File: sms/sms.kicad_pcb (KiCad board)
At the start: 2 copper layers, 17.5 x 65 mm, 3 parts, among them J1 Sega_GG_Cartridge, J2 Sega_SMS_Cartridge

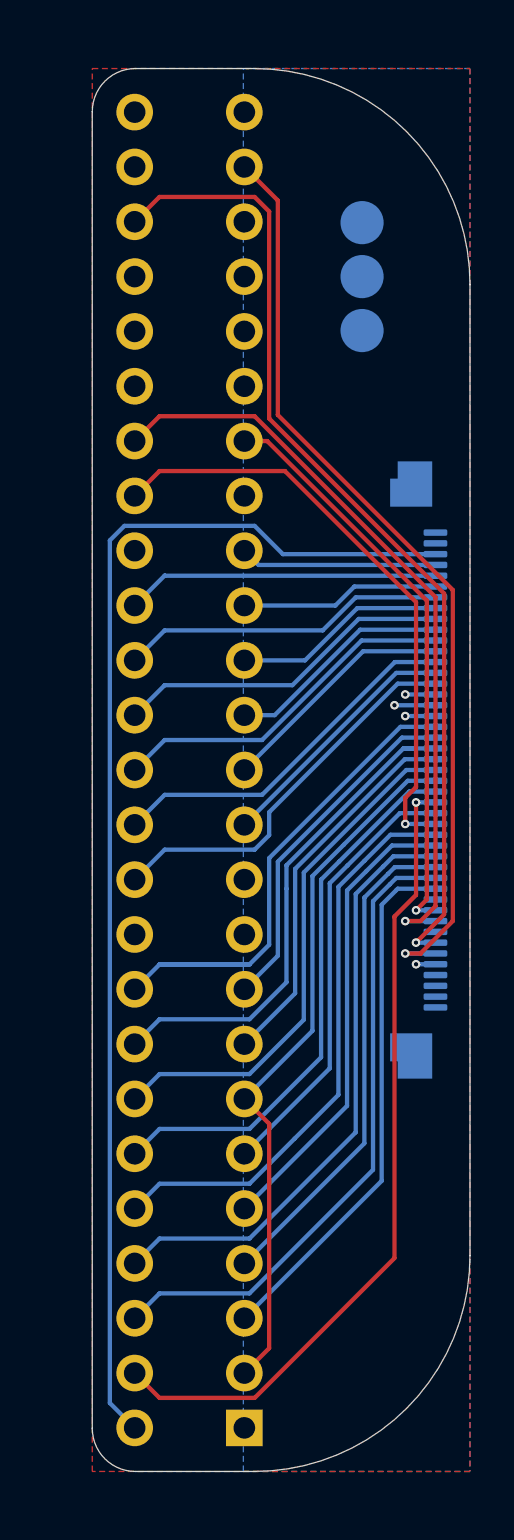
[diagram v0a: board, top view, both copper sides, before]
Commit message: Widen via holes
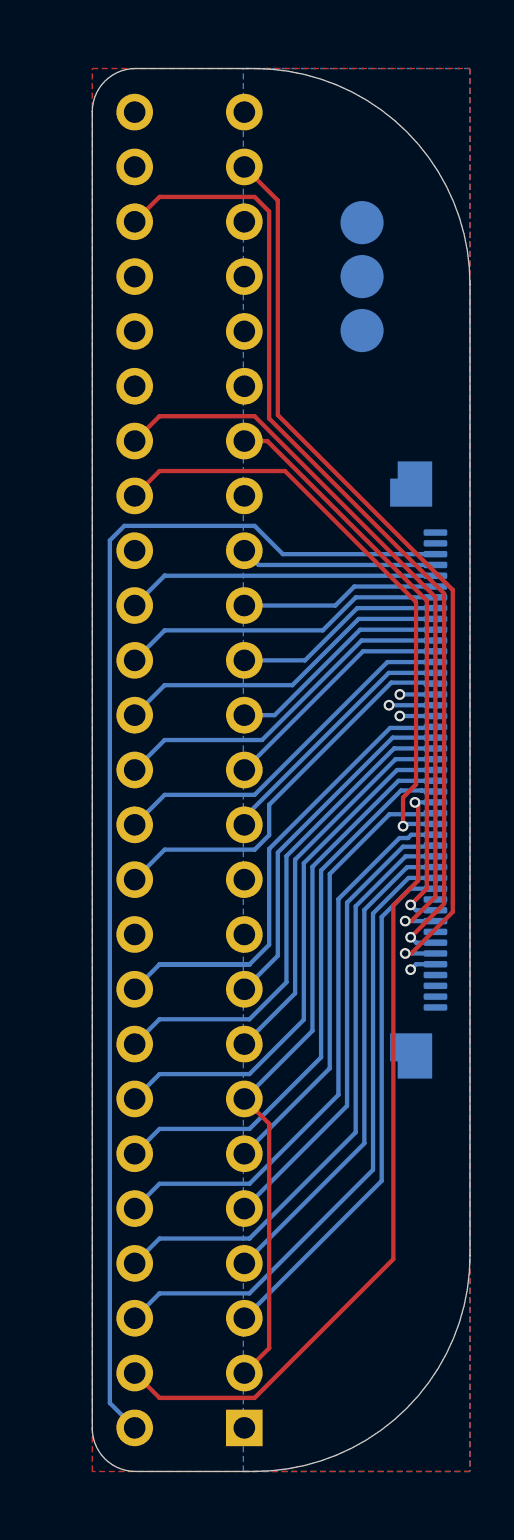
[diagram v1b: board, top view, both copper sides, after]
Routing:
- net GND: track 5.60 -> 6.70 mm

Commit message: Fix SMS pin ordering
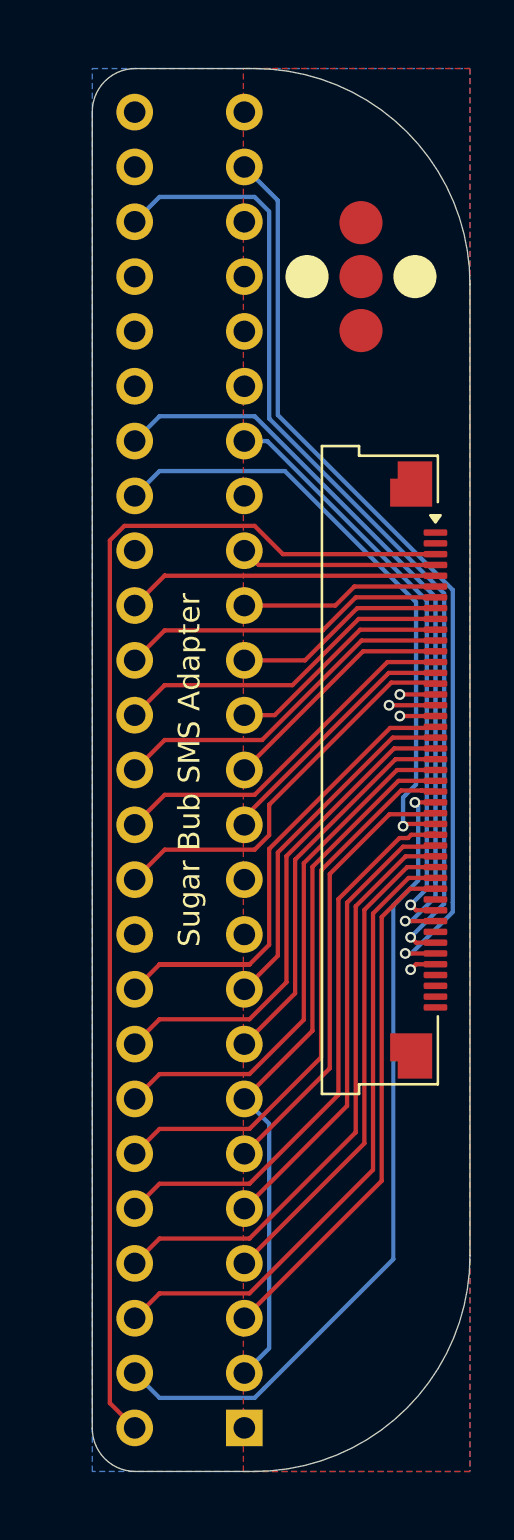
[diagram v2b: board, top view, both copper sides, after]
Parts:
- J1: footprint SugarBub:Amphenol_F32Q-1A7x1-11045_1x45-1MP_P0.5mm_HorizontalReversed -> Connector_FFC-FPC:Amphenol_F32Q-1A7x1-11045_1x45-1MP_P0.5mm_Horizontal; moved to F.Cu
- TP1: moved to F.Cu
- turned J1 to -90 degrees
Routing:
- added copper zone on F.Cu, net +5V
- added copper zone on B.Cu, net GND
- removed copper zone on B.Cu, net +5V
- removed copper zone on F.Cu, net GND

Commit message: Redo SMS adapter
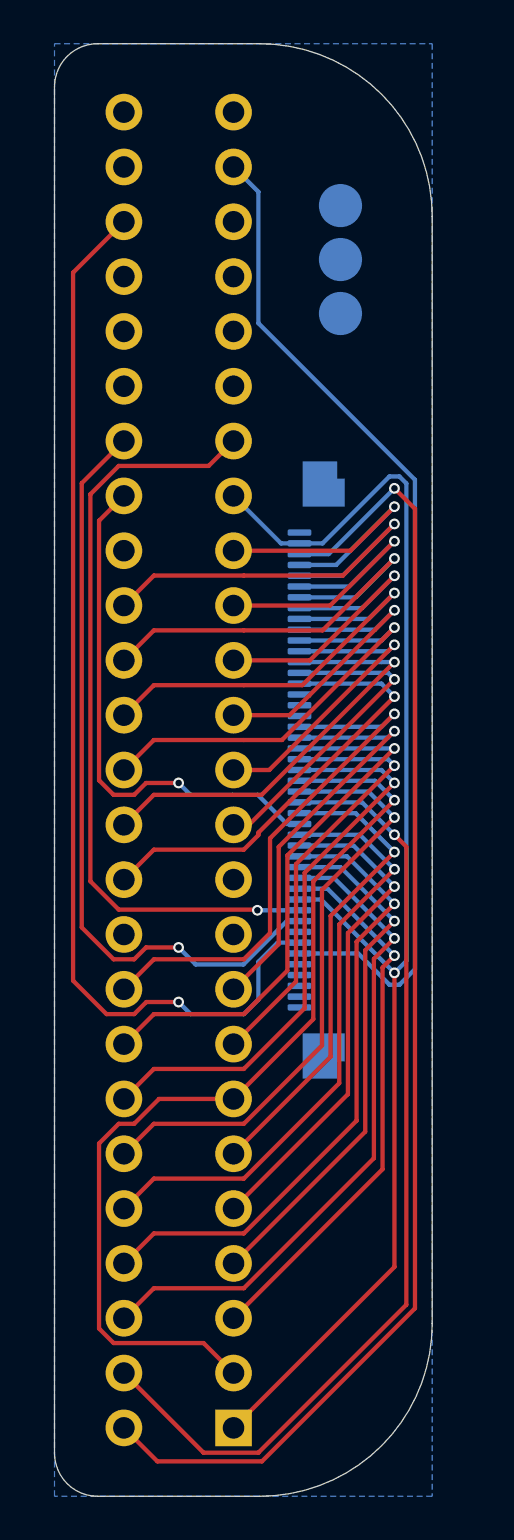
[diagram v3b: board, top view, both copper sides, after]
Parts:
- J1, TP1: moved to B.Cu
- moved TP1 1.24 mm to (109.5, 76.3)
- moved J1 0.50 mm to (110.5, 100.0)
- moved J2 0.50 mm to (104.5, 130.5)
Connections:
- J1 pad 42: +5V -> unconnected-(J1-Pin_42-Pad42)
- J1 pad 43: +5V -> unconnected-(J1-Pin_43-Pad43)
- TP1 pad 1: +5V -> unconnected-(TP1-Pad1)
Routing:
- net +5V: track 0.00 -> 63.2 mm, vias 0 -> 1
- net /CE: track 33.1 -> 44.4 mm, vias 0 -> 1
- net /M1: track 27.2 -> 35.8 mm
- net /RD: track 37.8 -> 44.5 mm
- net GND: track 6.70 -> 0.00 mm, vias 4 -> 0
- net /A7: track 14.5 -> 19.5 mm, vias 0 -> 1
- net /A6: track 9.22 -> 14.0 mm, vias 0 -> 1
- net /A12: track 9.13 -> 13.8 mm, vias 0 -> 1
- net /A5: track 15.1 -> 19.6 mm, vias 0 -> 1
- net /RST: track 45.9 -> 50.1 mm
- net /A4: track 9.86 -> 14.1 mm, vias 0 -> 1
- net /A3: track 15.8 -> 19.8 mm, vias 0 -> 1
- net CLK: track 42.9 -> 46.9 mm, vias 1 -> 0
- net /A15: track 28.2 -> 24.2 mm
- net /A2: track 10.5 -> 14.2 mm, vias 0 -> 1
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- removed copper zone on F.Cu, net +5V
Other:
- board size 17.5 x 65 mm -> 17.5 x 67.3 mm

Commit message: Add /Refresh to SMS and shrink logo
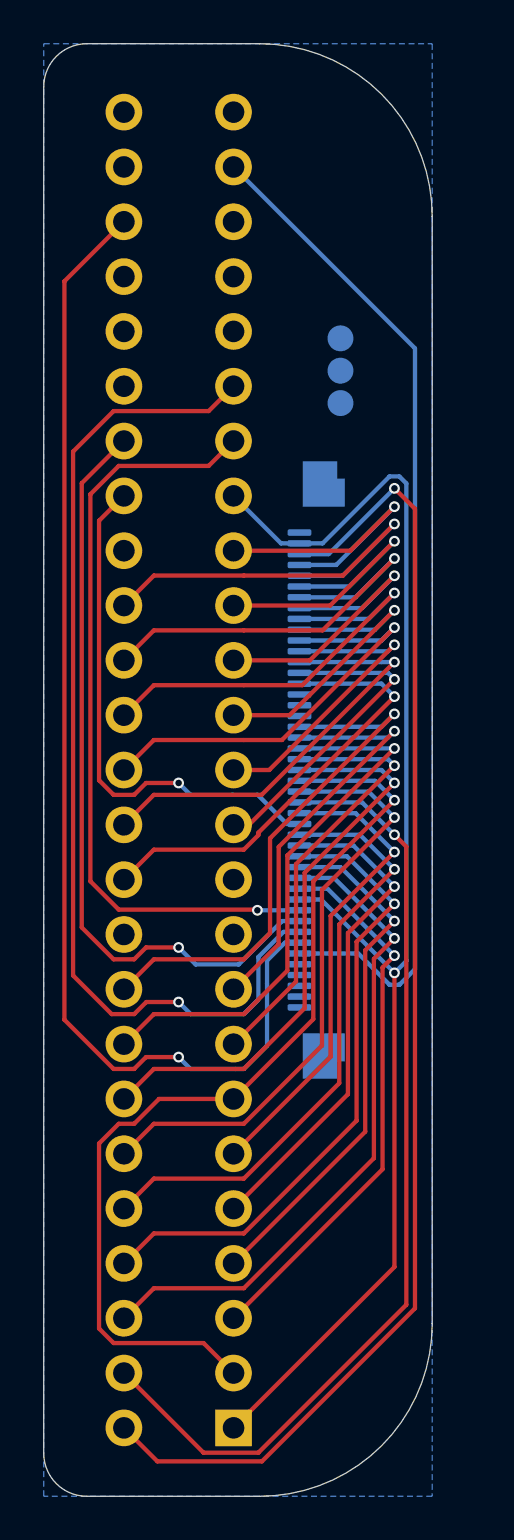
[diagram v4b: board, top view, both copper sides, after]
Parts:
- TP1: footprint SugarBub:SugarBub_Symbol -> SugarBub:SugarBub_Symbol_4.2mm
- moved TP1 5.15 mm to (109.5, 81.5), turned to -90 degrees
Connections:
- J1 pad 38: unconnected-(J1-Pin_38-Pad38) -> /RFSH
- J2 pad 39: unconnected-(J2-Pin_39-Pad39) -> /RFSH
- TP1 pad 1: unconnected-(TP1-Pad1) -> GND
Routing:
- net /RFSH: track 0.00 -> 47.4 mm, vias 0 -> 1
- net /RST: track 50.1 -> 55.1 mm
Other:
- board size 17.5 x 67.3 mm -> 18 x 67.3 mm
- board text added: "1"
- board text added: "2"
- board text added: "49"
- board text added: "50"

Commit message: Move SMS adapter text to center
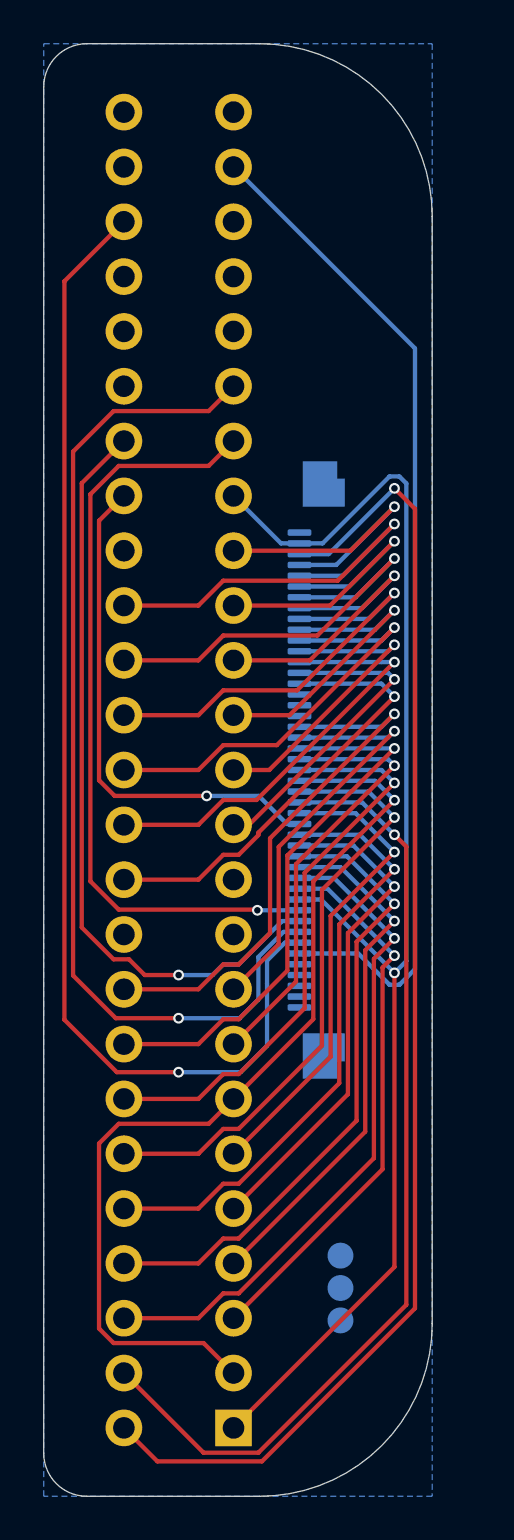
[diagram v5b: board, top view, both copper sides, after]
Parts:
- moved TP1 42.5 mm to (109.5, 124.0)
